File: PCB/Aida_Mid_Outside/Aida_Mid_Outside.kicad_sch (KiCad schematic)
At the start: 5 parts

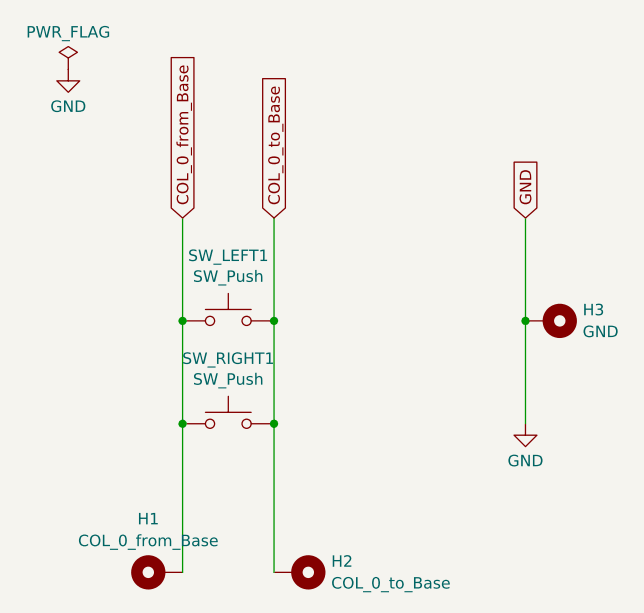
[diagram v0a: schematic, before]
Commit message: テストポイントを追加、配置した。
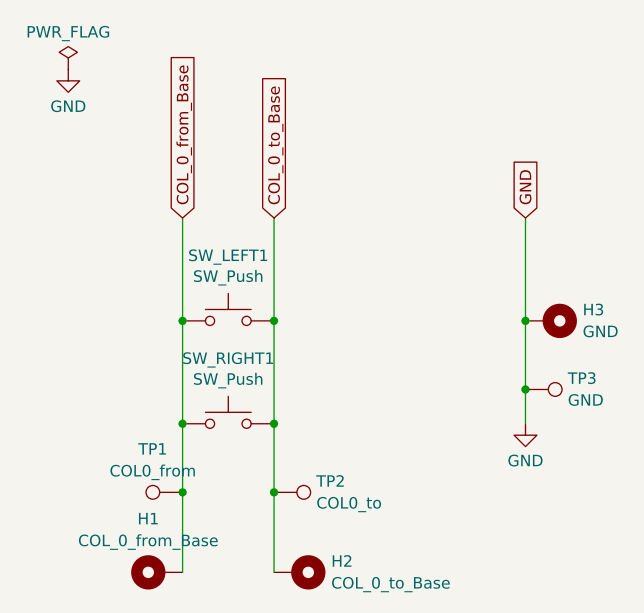
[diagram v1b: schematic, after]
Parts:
- added TP1: COL0_from, Connector_PinHeader_2.00mm:PinHeader_1x01_P2.00mm_Vertical, symbol Connector:TestPoint
- added TP2: COL0_to, Connector_PinHeader_2.00mm:PinHeader_1x01_P2.00mm_Vertical, symbol Connector:TestPoint
- added TP3: GND, Connector_PinHeader_2.00mm:PinHeader_1x01_P2.00mm_Vertical, symbol Connector:TestPoint
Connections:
- net COL_0_from_Base: now also TP1.1
- net COL_0_to_Base: now also TP2.1
- net GND: now also TP3.1
